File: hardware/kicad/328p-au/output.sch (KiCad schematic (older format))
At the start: 12 parts

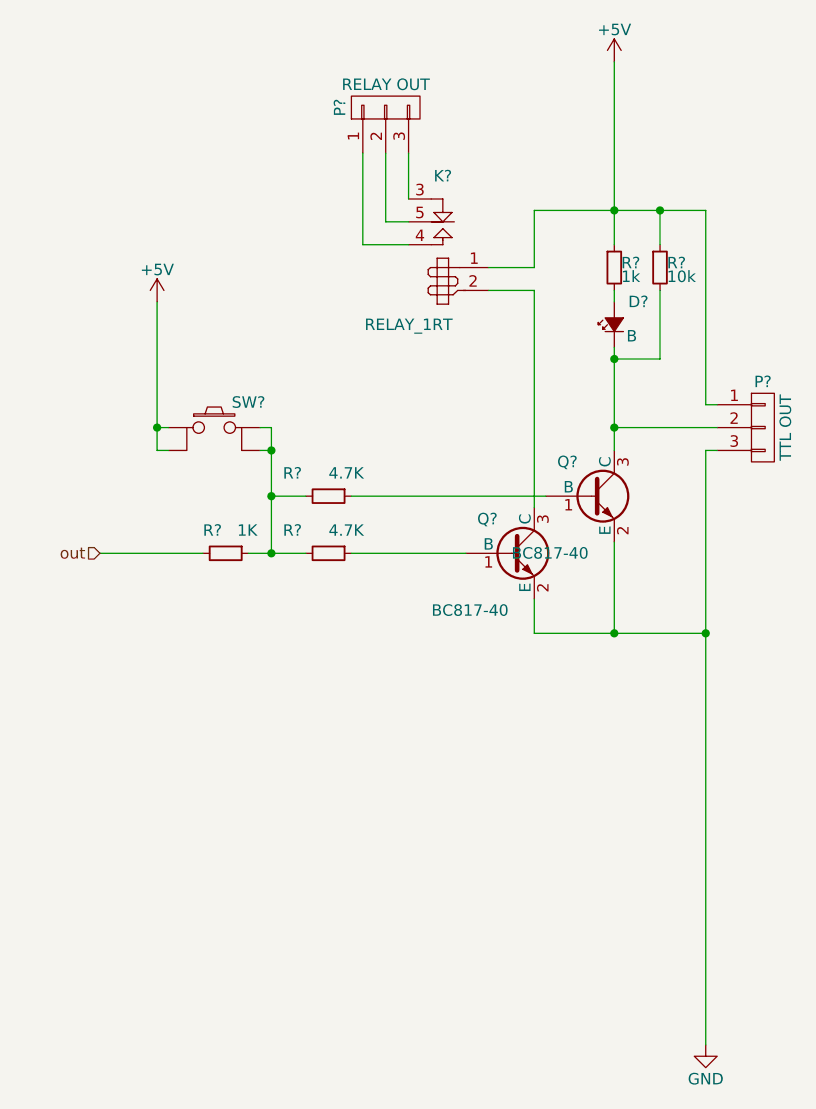
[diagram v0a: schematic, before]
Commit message: hardware/kicad/328p-au: separated collpits page, footprints assigned and imported to PCB
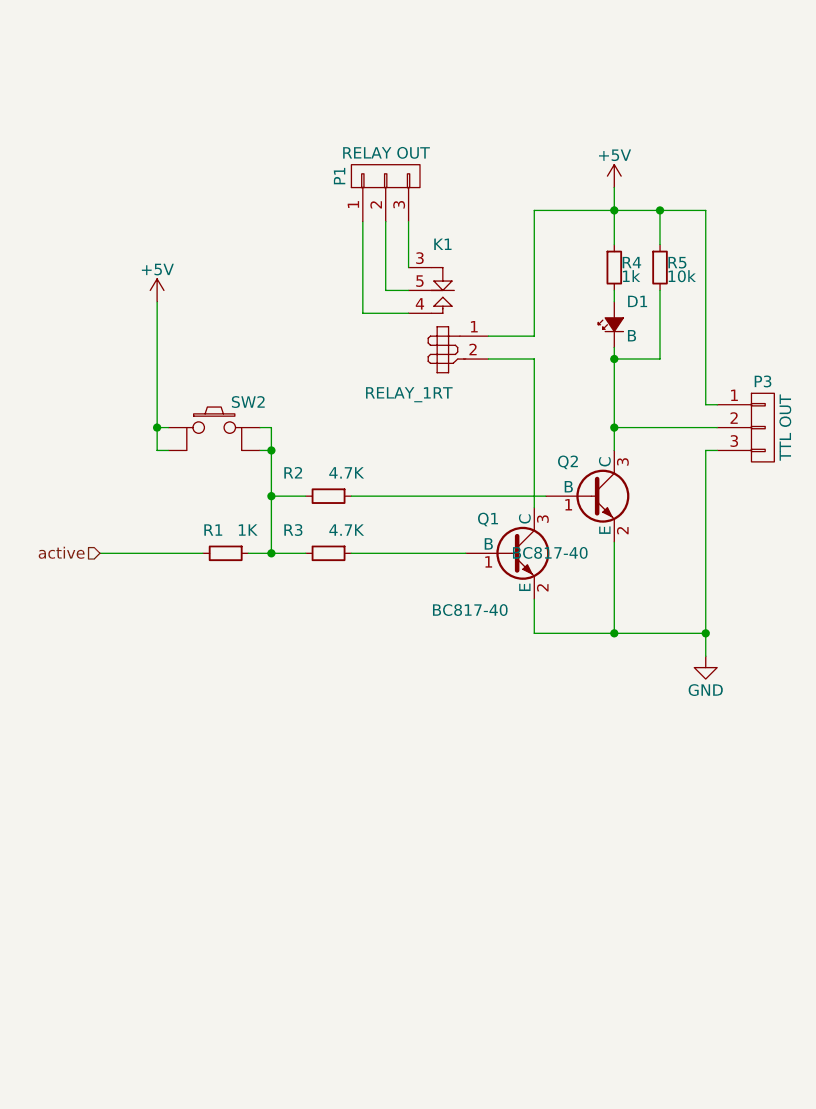
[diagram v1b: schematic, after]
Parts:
- D1: renamed from D?; footprint (none) -> gate433:SOD80C
- P1: renamed from P?; footprint (none) -> con-wago-508:W237-133
- P3: renamed from P?; footprint (none) -> Pin_Headers:Pin_Header_Straight_1x03
- Q1, Q2: renamed from Q?; footprint SOT-23 -> TO_SOT_Packages_SMD:SOT-23
- R1, R2, R3, R4, R5: renamed from R?; footprint (none) -> Resistors_SMD:R_0603_HandSoldering
- SW2: renamed from SW?; footprint (none) -> Buttons_Switches_ThroughHole:SW_TH_Tactile_Omron_B3F-10xx
- gave numbers to parts that had none: 1
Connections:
- net out renamed active
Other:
- moved on the sheet: K1, P1
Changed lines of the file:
@@
 $Descr A4 11693 8268
 encoding utf-8
-Sheet 2 2
+Sheet 2 3
 Title ""
 Date ""
@@
 $EndDescr
 $Comp
-L R_Small R?
+L R_Small R1
 U 1 1 575F77FE
 P 2150 4050
-F 0 "R?" V 2050 3950 50  0000 L CNN
+F 0 "R1" V 2050 3950 50  0000 L CNN
 F 1 "1K" V 2050 4100 50  0000 L CNN
-F 2 "" H 2150 4050 50  0001 C CNN
+F 2 "Resistors_SMD:R_0603_HandSoldering" H 2150 4050 50  0001 C CNN
 F 3 "" H 2150 4050 50  0000 C CNN
 	1    2150 4050
@@
 $EndComp
 $Comp
-L R_Small R?
+L R_Small R3
 U 1 1 575F7805
 P 2600 4050
-F 0 "R?" V 2500 3850 50  0000 L CNN
+F 0 "R3" V 2500 3850 50  0000 L CNN
 F 1 "4.7K" V 2500 4050 50  0000 L CNN
-F 2 "" H 2600 4050 50  0001 C CNN
+F 2 "Resistors_SMD:R_0603_HandSoldering" H 2600 4050 50  0001 C CNN
 F 3 "" H 2600 4050 50  0000 C CNN
 	1    2600 4050
@@
 $EndComp
 $Comp
-L R_Small R?
+L R_Small R2
 U 1 1 575F780C
 P 2600 3800
-F 0 "R?" V 2500 3600 50  0000 L CNN
+F 0 "R2" V 2500 3600 50  0000 L CNN
 F 1 "4.7K" V 2500 3800 50  0000 L CNN
-F 2 "" H 2600 3800 50  0001 C CNN
+F 2 "Resistors_SMD:R_0603_HandSoldering" H 2600 3800 50  0001 C CNN
 F 3 "" H 2600 3800 50  0000 C CNN
 	1    2600 3800
@@
 $EndComp
 $Comp
-L GND #PWR?
+L GND #PWR017
 U 1 1 575F7813
-P 4250 6200
-F 0 "#PWR?" H 4250 5950 50  0001 C CNN
-F 1 "GND" H 4250 6050 50  0000 C CNN
-F 2 "" H 4250 6200 50  0000 C CNN
-F 3 "" H 4250 6200 50  0000 C CNN
-	1    4250 6200
-	1    0    0    -1
-$EndComp
-$Comp
-L Led_Small D?
+P 4250 4500
+F 0 "#PWR017" H 4250 4250 50  0001 C CNN
+F 1 "GND" H 4250 4350 50  0000 C CNN
+F 2 "" H 4250 4500 50  0000 C CNN
+F 3 "" H 4250 4500 50  0000 C CNN
+	1    4250 4500
+	1    0    0    -1
+$EndComp
+$Comp
+L Led_Small D1
 U 1 1 575F7819
 P 3850 3050
-F 0 "D?" V 3950 2900 50  0000 L CNN
+F 0 "D1" V 3950 2900 50  0000 L CNN
 F 1 "B" V 3800 2950 50  0000 L CNN
-F 2 "" V 3850 3050 50  0001 C CNN
+F 2 "gate433:SOD80C" V 3850 3050 50  0001 C CNN
 F 3 "" V 3850 3050 50  0000 C CNN
 	1    3850 3050
@@
 $EndComp
 $Comp
-L R_Small R?
+L R_Small R4
 U 1 1 575F7820
 P 3850 2800
-F 0 "R?" H 3880 2820 50  0000 L CNN
+F 0 "R4" H 3880 2820 50  0000 L CNN
 F 1 "1k" H 3880 2760 50  0000 L CNN
-F 2 "" H 3850 2800 50  0001 C CNN
+F 2 "Resistors_SMD:R_0603_HandSoldering" H 3850 2800 50  0001 C CNN
 F 3 "" H 3850 2800 50  0000 C CNN
 	1    3850 2800
@@
 $EndComp
 $Comp
-L CONN_01X03 P?
+L CONN_01X03 P3
 U 1 1 575F7827
 P 4500 3500
-F 0 "P?" H 4500 3700 50  0000 C CNN
+F 0 "P3" H 4500 3700 50  0000 C CNN
 F 1 "TTL OUT" V 4600 3500 50  0000 C CNN
-F 2 "" H 4500 3500 50  0001 C CNN
+F 2 "Pin_Headers:Pin_Header_Straight_1x03" H 4500 3500 50  0001 C CNN
 F 3 "" H 4500 3500 50  0000 C CNN
 	1    4500 3500
@@
 $EndComp
 $Comp
-L RELAY_1RT K?
+L RELAY_1RT K1
 U 1 1 575F782E
-P 3100 2550
-F 0 "K?" H 3100 2700 50  0000 C CNN
-F 1 "RELAY_1RT" H 3250 2050 50  0000 C CNN
-F 2 "relays:SRD-SL-C" H 3050 2550 50  0001 C CNN
-F 3 "" H 3050 2550 50  0000 C CNN
-	1    3100 2550
+P 3100 2850
+F 0 "K1" H 3100 3000 50  0000 C CNN
+F 1 "RELAY_1RT" H 3250 2350 50  0000 C CNN
+F 2 "relays:SRD-SL-C" H 3050 2850 50  0001 C CNN
+F 3 "" H 3050 2850 50  0000 C CNN
+	1    3100 2850
 	-1   0    0    -1
 $EndComp
 $Comp
-L +5V #PWR?
+L +5V #PWR018
 U 1 1 575F7835
-P 3850 1900
-F 0 "#PWR?" H 3850 1750 50  0001 C CNN
-F 1 "+5V" H 3850 2040 50  0000 C CNN
-F 2 "" H 3850 1900 50  0000 C CNN
-F 3 "" H 3850 1900 50  0000 C CNN
-	1    3850 1900
-	1    0    0    -1
-$EndComp
-$Comp
-L CONN_01X03 P?
+P 3850 2450
+F 0 "#PWR018" H 3850 2300 50  0001 C CNN
+F 1 "+5V" H 3850 2590 50  0000 C CNN
+F 2 "" H 3850 2450 50  0000 C CNN
+F 3 "" H 3850 2450 50  0000 C CNN
+	1    3850 2450
+	1    0    0    -1
+$EndComp
+$Comp
+L CONN_01X03 P1
 U 1 1 575F783B
-P 2850 2100
-F 0 "P?" H 2850 2300 50  0000 C CNN
-F 1 "RELAY OUT" V 2950 2100 50  0000 C CNN
-F 2 "" H 2850 2100 50  0001 C CNN
-F 3 "" H 2850 2100 50  0000 C CNN
-	1    2850 2100
+P 2850 2400
+F 0 "P1" H 2850 2600 50  0000 C CNN
+F 1 "RELAY OUT" V 2950 2400 50  0000 C CNN
+F 2 "con-wago-508:W237-133" H 2850 2400 50  0001 C CNN
+F 3 "" H 2850 2400 50  0000 C CNN
+	1    2850 2400
 	0    -1   -1   0
 $EndComp
 $Comp
-L TACTILE_SW SW?
+L TACTILE_SW SW2
 U 1 1 575F7842
 P 2100 3500
-F 0 "SW?" H 2250 3610 50  0000 C CNN
+F 0 "SW2" H 2250 3610 50  0000 C CNN
 F 1 "TACTILE_SW" H 2120 3360 50  0001 C CNN
-F 2 "" H 2100 3500 50  0001 C CNN
+F 2 "Buttons_Switches_ThroughHole:SW_TH_Tactile_Omron_B3F-10xx" H 2100 3500 50  0001 C CNN
 F 3 "" H 2100 3500 50  0000 C CNN
 	1    2100 3500
@@
 $EndComp
 Wire Wire Line
-	2250 4050 2350 4050
-Wire Wire Line
-	2350 4050 2500 4050
-Wire Wire Line
-	2350 3500 2350 3600
-Wire Wire Line
-	2350 3600 2350 3800
-Wire Wire Line
-	2350 3800 2350 4050
+	2250 4050 2500 4050
+Wire Wire Line
+	2350 3500 2350 4050
 Wire Wire Line
 	2350 3800 2500 3800
@@
 	2700 3800 3550 3800
 Wire Wire Line
-	3850 3150 3850 3200
-Wire Wire Line
-	3850 3200 3850 3500
-Wire Wire Line
-	3850 3500 3850 3600
+	3850 3150 3850 3600
 Wire Wire Line
 	3850 2950 3850 2900
 Wire Wire Line
-	3500 2550 3850 2550
-Wire Wire Line
-	3850 2550 4050 2550
-Wire Wire Line
-	4050 2550 4250 2550
-Wire Wire Line
-	3850 1900 3850 2550
-Wire Wire Line
-	3850 2550 3850 2700
+	3500 2550 4250 2550
+Wire Wire Line
+	3850 2450 3850 2700
 Wire Wire Line
 	4300 3500 3850 3500
 Connection ~ 3850 3500
 Wire Wire Line
-	3500 3850 3500 2900
-Wire Wire Line
-	3500 2800 3500 2550
+	3500 3850 3500 3200
+Wire Wire Line
+	3500 3100 3500 2550
 Connection ~ 3850 2550
 Wire Wire Line
-	2950 2300 2950 2500
-Wire Wire Line
-	2850 2300 2850 2600
-Wire Wire Line
-	2850 2600 2950 2600
-Wire Wire Line
-	2750 2300 2750 2700
-Wire Wire Line
-	2750 2700 2950 2700
+	2950 2600 2950 2800
+Wire Wire Line
+	2850 2600 2850 2900
+Wire Wire Line
+	2850 2900 2950 2900
+Wire Wire Line
+	2750 2600 2750 3000
+Wire Wire Line
+	2750 3000 2950 3000
 Wire Wire Line
 	1600 4050 2050 4050
 Wire Wire Line
-	4250 3600 4250 4400
-Wire Wire Line
-	4250 4400 4250 6200
+	4250 3600 4250 4500
 Wire Wire Line
 	4250 3600 4300 3600
@@
 	1850 3600 1900 3600
 Wire Wire Line
-	1850 2950 1850 3500
-Wire Wire Line
-	1850 3500 1850 3600
+	1850 2950 1850 3600
 Wire Wire Line
 	1850 3500 1900 3500
 $Comp
-L +5V #PWR?
+L +5V #PWR019
 U 1 1 575F7873
 P 1850 2950
-F 0 "#PWR?" H 1850 2800 50  0001 C CNN
+F 0 "#PWR019" H 1850 2800 50  0001 C CNN
 F 1 "+5V" H 1850 3090 50  0000 C CNN
 F 2 "" H 1850 2950 50  0000 C CNN
@@
 Connection ~ 1850 3500
 $Comp
-L R_Small R?
+L R_Small R5
 U 1 1 575F787A
 P 4050 2800
-F 0 "R?" H 4080 2820 50  0000 L CNN
+F 0 "R5" H 4080 2820 50  0000 L CNN
 F 1 "10k" H 4080 2760 50  0000 L CNN
-F 2 "" H 4050 2800 50  0001 C CNN
+F 2 "Resistors_SMD:R_0603_HandSoldering" H 4050 2800 50  0001 C CNN
 F 3 "" H 4050 2800 50  0000 C CNN
 	1    4050 2800
@@
 Connection ~ 3850 3200
 Wire Wire Line
-	3500 2800 3300 2800
-Wire Wire Line
-	3500 2900 3300 2900
-$Comp
-L BC817-40 Q?
+	3500 3100 3300 3100
+Wire Wire Line
+	3500 3200 3300 3200
+$Comp
+L BC817-40 Q1
 U 1 1 575F7888
 P 3400 4050
-F 0 "Q?" H 3250 4200 50  0000 L CNN
+F 0 "Q1" H 3250 4200 50  0000 L CNN
 F 1 "BC817-40" H 3050 3800 50  0000 L CNN
-F 2 "SOT-23" H 3600 3975 50  0001 L CIN
+F 2 "TO_SOT_Packages_SMD:SOT-23" H 3600 3975 50  0001 L CIN
 F 3 "" H 3400 4050 50  0000 L CNN
 	1    3400 4050
@@
 $EndComp
 $Comp
-L BC817-40 Q?
+L BC817-40 Q2
 U 1 1 575F788F
 P 3750 3800
-F 0 "Q?" H 3600 3950 50  0000 L CNN
+F 0 "Q2" H 3600 3950 50  0000 L CNN
 F 1 "BC817-40" H 3400 3550 50  0000 L CNN
-F 2 "SOT-23" H 3950 3725 50  0001 L CIN
+F 2 "TO_SOT_Packages_SMD:SOT-23" H 3950 3725 50  0001 L CIN
 F 3 "" H 3750 3800 50  0000 L CNN
 	1    3750 3800
@@
 	4250 2550 4250 3400
 Wire Wire Line
-	3500 4400 3850 4400
-Wire Wire Line
-	3850 4400 4250 4400
+	3500 4400 4250 4400
 Connection ~ 4250 4400
 Connection ~ 3850 4400
 Text HLabel 1600 4050 0    50   Input ~ 0
-out
+active
 $EndSCHEMATC

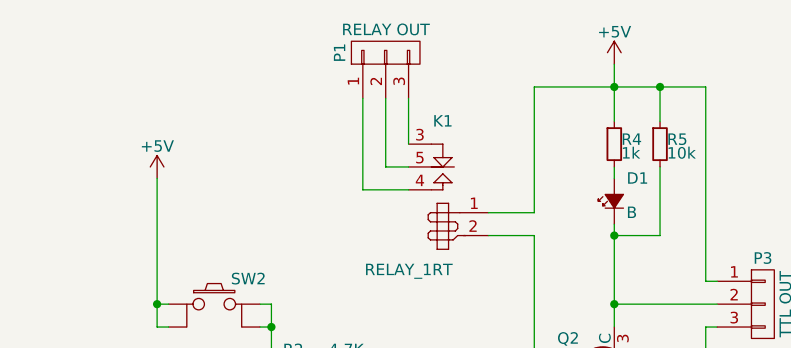
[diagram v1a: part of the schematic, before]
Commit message: hardware/kicad/328p-au: use 3x2 jumper block for frequency selection
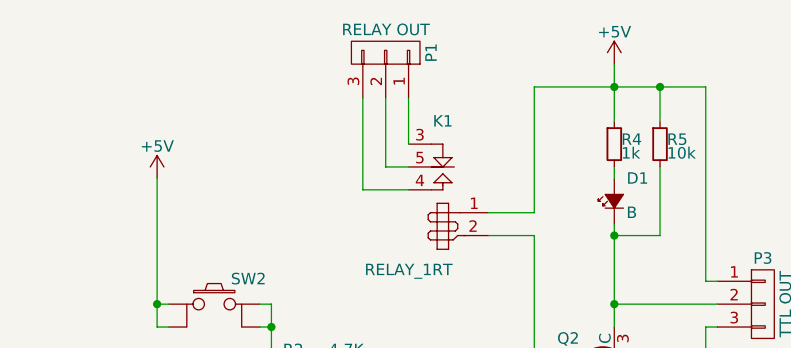
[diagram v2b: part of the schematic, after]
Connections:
- net at K1.3 (R1): now also P1.1 (P1); no longer P1.3 (P3)
- net at K1.4 (T1): now also P1.3 (P3); no longer P1.1 (P1)
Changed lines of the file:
@@
 LIBS:gdt
 LIBS:button
+LIBS:jumpers
 LIBS:cardetector_328p-au-cache
 EELAYER 25 0
@@
 $EndComp
 $Comp
-L GND #PWR017
+L GND #PWR19
 U 1 1 575F7813
 P 4250 4500
-F 0 "#PWR017" H 4250 4250 50  0001 C CNN
+F 0 "#PWR19" H 4250 4250 50  0001 C CNN
 F 1 "GND" H 4250 4350 50  0000 C CNN
 F 2 "" H 4250 4500 50  0000 C CNN
@@
 $EndComp
 $Comp
-L +5V #PWR018
+L +5V #PWR18
 U 1 1 575F7835
 P 3850 2450
-F 0 "#PWR018" H 3850 2300 50  0001 C CNN
+F 0 "#PWR18" H 3850 2300 50  0001 C CNN
 F 1 "+5V" H 3850 2590 50  0000 C CNN
 F 2 "" H 3850 2450 50  0000 C CNN
@@
 F 3 "" H 2850 2400 50  0000 C CNN
 	1    2850 2400
-	0    -1   -1   0
+	0    1    -1   0
 $EndComp
 $Comp
@@
 	1850 3500 1900 3500
 $Comp
-L +5V #PWR019
+L +5V #PWR17
 U 1 1 575F7873
 P 1850 2950
-F 0 "#PWR019" H 1850 2800 50  0001 C CNN
+F 0 "#PWR17" H 1850 2800 50  0001 C CNN
 F 1 "+5V" H 1850 3090 50  0000 C CNN
 F 2 "" H 1850 2950 50  0000 C CNN
